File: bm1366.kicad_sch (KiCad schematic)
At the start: 54 parts, among them J3 Conn_01x05, U1 25MHz, U14 BM1366_mode1, U2 TXB0104RGYR, U5 MCP1824T-1802E, U6 MCP1824T-0802E

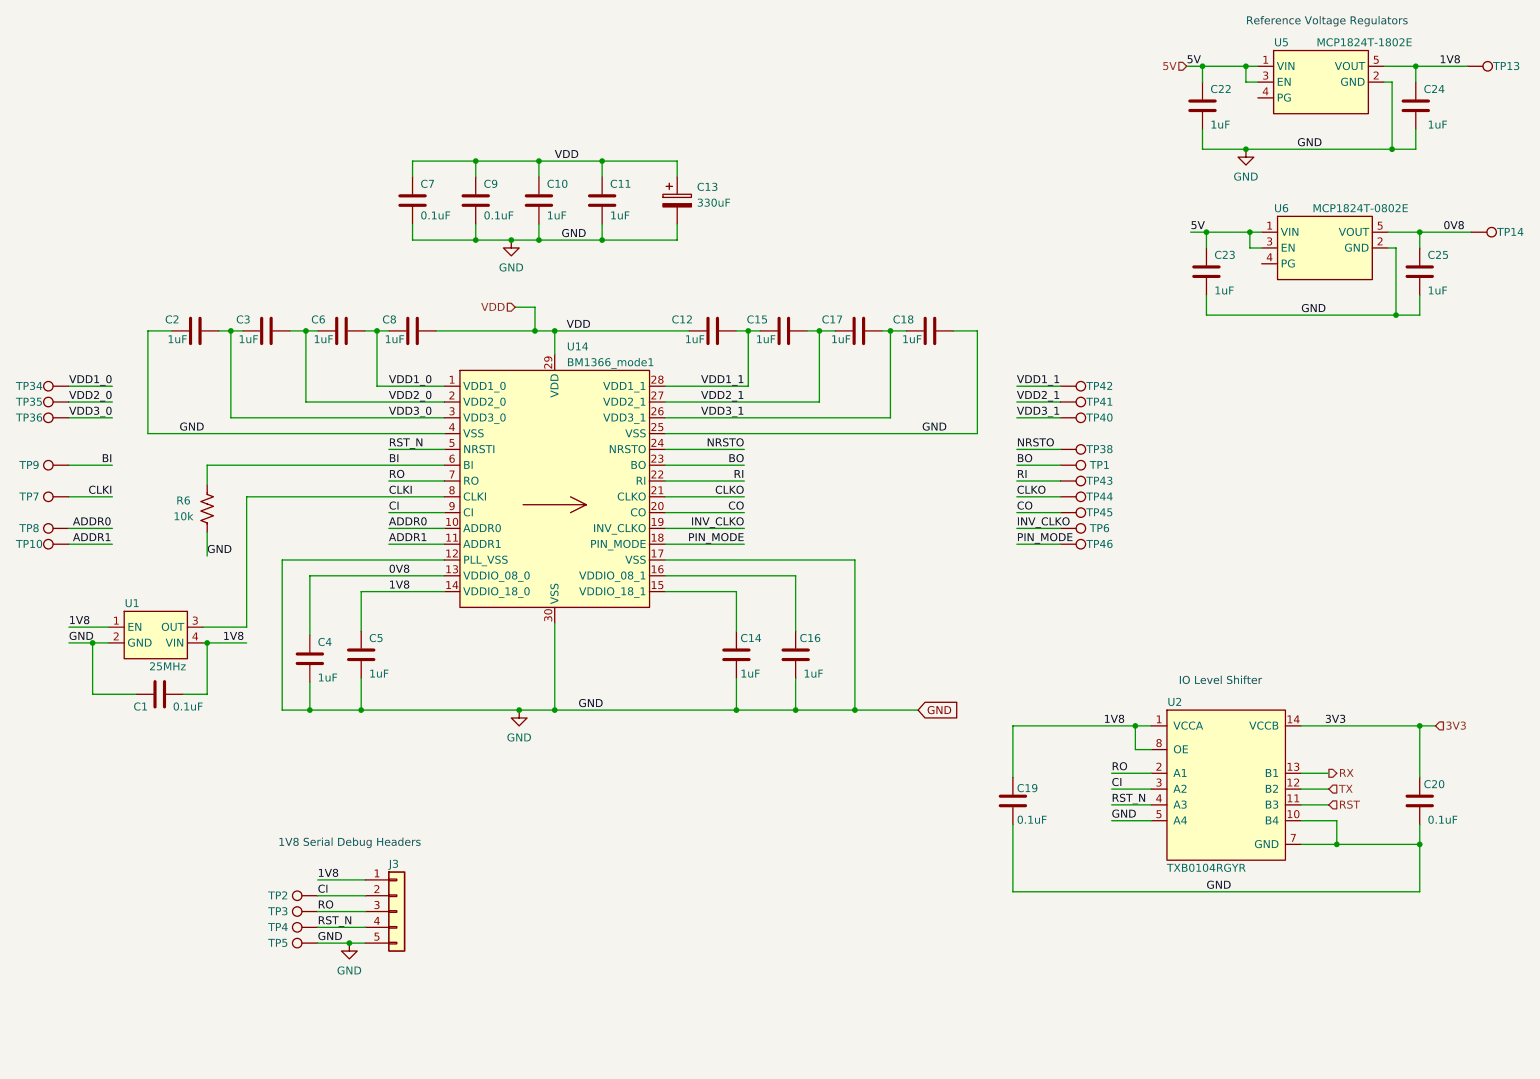
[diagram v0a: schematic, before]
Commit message: routing for ASIC board
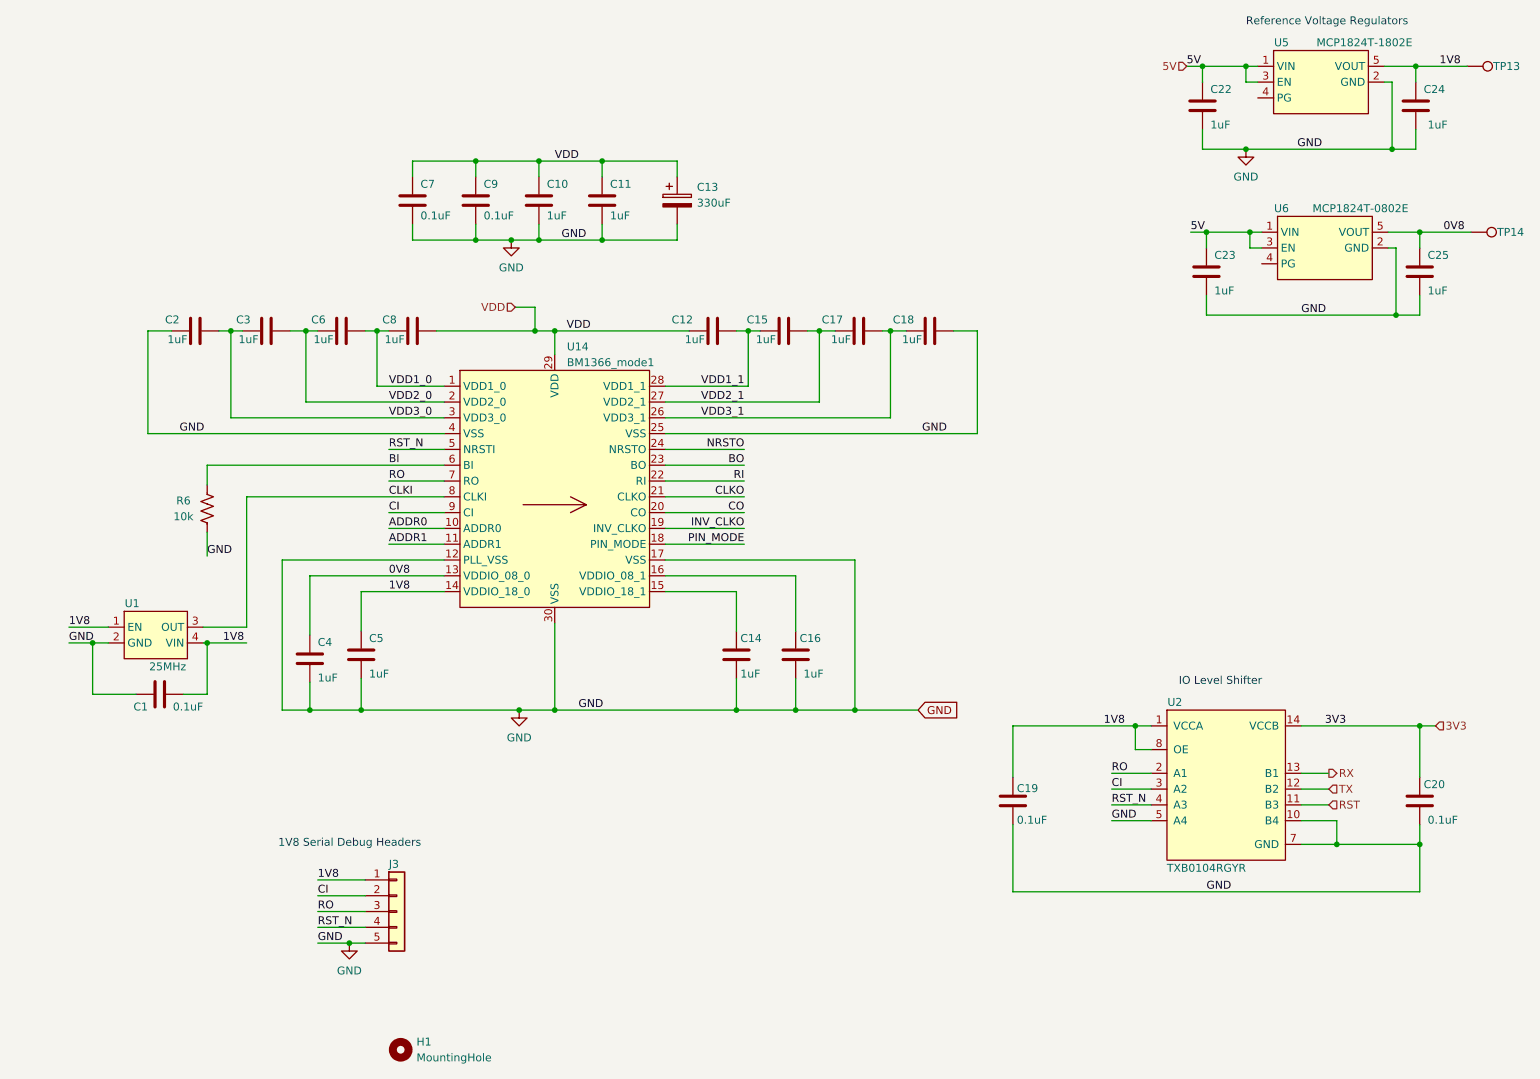
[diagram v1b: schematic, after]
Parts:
- removed TP1, TP10, TP2, TP3, TP34, TP35, TP36, TP38, TP4, TP40, TP41, TP42, TP43, TP44, TP45, TP46, TP5, TP6, TP7, TP8, TP9: TestPoint, TestPoint:TestPoint_Pad_D1.5mm, symbol Connector:TestPoint
- added H1: MountingHole, bitaxe:heatsink_mount_bridge, symbol Mechanical:MountingHole
- C1, C19, C20, C7, C9: LCSC (none) -> C1525
- C10, C11, C12, C14, C15, C16, C17, C18, C2, C22, C23, C24, C25, C3, C4, C5, C6, C8: LCSC (none) -> C52923
- C13: LCSC (none) -> C347551
- R6: LCSC (none) -> C25744
- U1: LCSC (none) -> C507380
- U2: LCSC (none) -> C400708
- U5: LCSC (none) -> C625462
- U6: LCSC (none) -> C625460

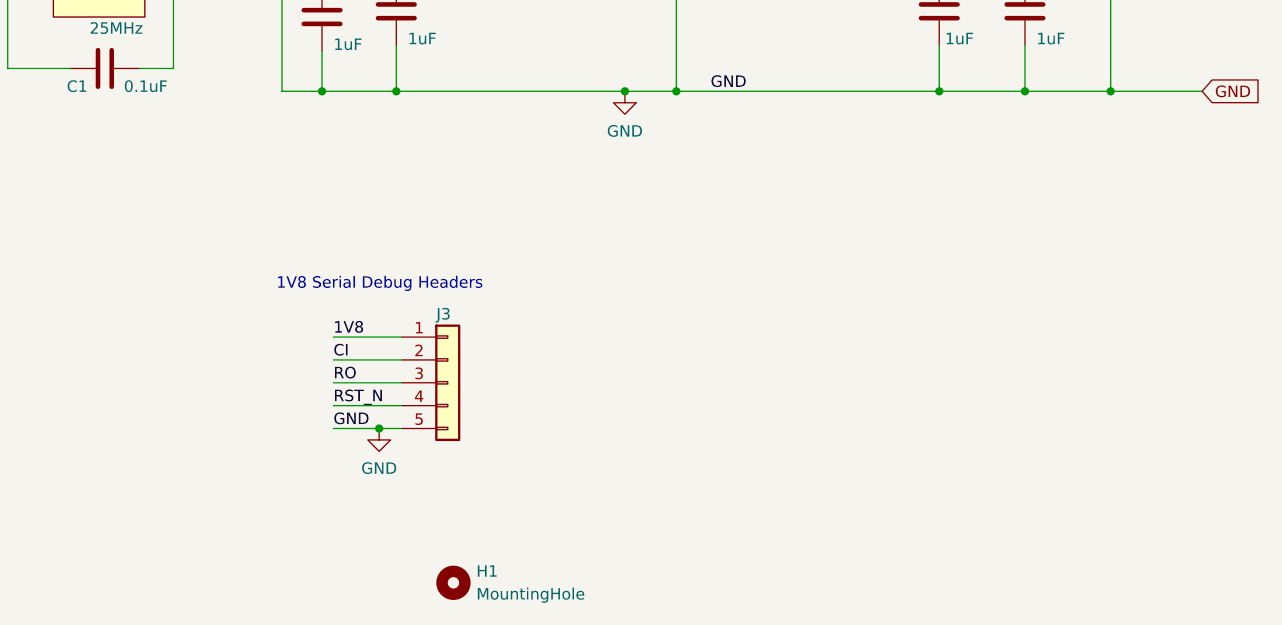
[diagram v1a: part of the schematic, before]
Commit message: revert  to 4 layer-board routing
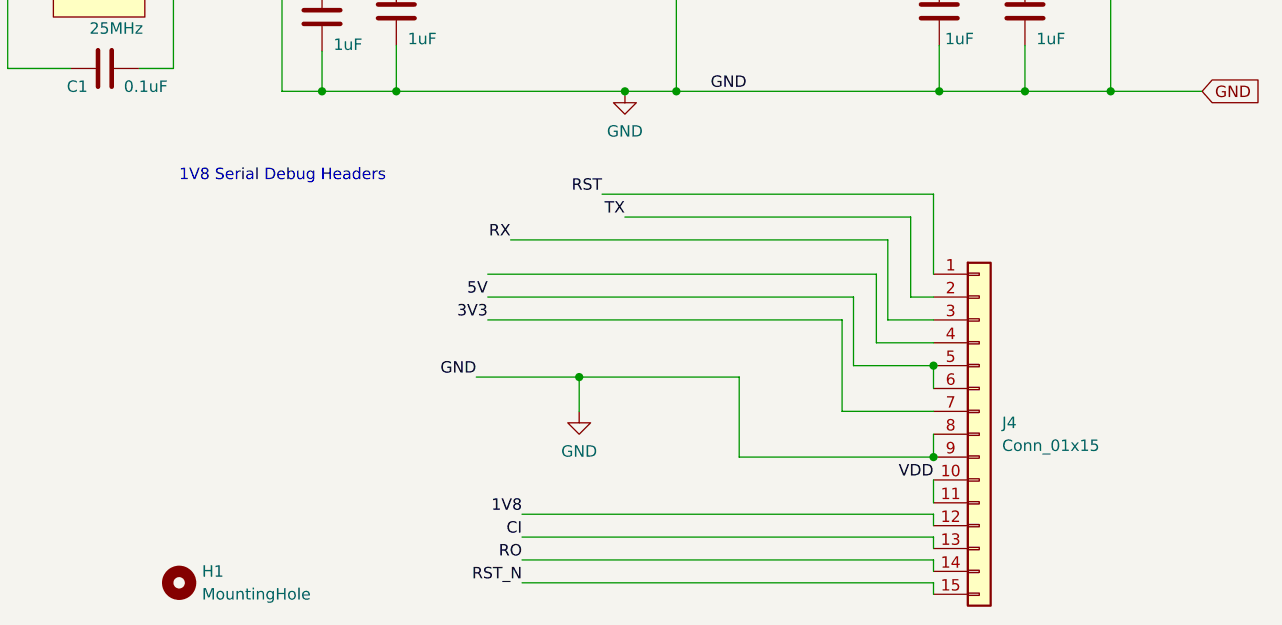
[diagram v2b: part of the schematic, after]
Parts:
- removed J3: Conn_01x05, Connector_PinHeader_2.54mm:PinHeader_1x05_P2.54mm_Vertical, symbol Connector_Generic:Conn_01x05
- added J4: Conn_01x15, Connector_JST:JST_XA_B15B-XASK-1_1x15_P2.50mm_Vertical, symbol Connector_Generic:Conn_01x15
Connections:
- net 1V8: now also J4.12 (Pin_12)
- net 3V3: now also J4.7 (Pin_7)
- net 5V: now also J4.5 (Pin_5), J4.6 (Pin_6)
- net CI: now also J4.13 (Pin_13)
- net GND: now also J4.8 (Pin_8), J4.9 (Pin_9)
- net RO: now also J4.14 (Pin_14)
- net RST: now also J4.1 (Pin_1)
- net RST_N: now also J4.15 (Pin_15)
- net RX: now also J4.3 (Pin_3)
- net TX: now also J4.2 (Pin_2)
- net VDD: now also J4.10 (Pin_10), J4.11 (Pin_11)
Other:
- moved on the sheet: H1
